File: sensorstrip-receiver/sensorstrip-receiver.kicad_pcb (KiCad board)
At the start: 2 copper layers, 40 x 12 mm, 8 parts, among them J1 Conn_01x02_MountingPin, J2 Conn_01x02_MountingPin

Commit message: fix humongous oversight
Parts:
- added ?: , , F.Cu at (133.2, 52.6)
- added ?: , , F.Cu at (105.0, 52.6)
- added ?: , , F.Cu at (106.9, 52.6)
- added ?: , , F.Cu at (135.0, 52.8)
- moved D1 12.0 mm to (114.0, 58.5)
- moved D3 12.0 mm to (126.0, 58.5)
- moved D2 0.50 mm to (120.0, 58.5)
- moved J2 0.10 mm to (106.0, 53.3)
- renumbered D3 to D1, D1 to D3
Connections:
- D1 pad 2: /LEDs -> /D1+
- D2 pad 1: GND -> /D1+
- D2 pad 2: /LEDs -> /D2+
- D3 pad 1: GND -> /D2+
- D3 pad 2: /LEDs -> /D3+
- R1 pad 1: /LEDs -> /D3+
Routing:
- net /LEDs: track 27.7 -> 0.00 mm
- net /D3+: track 0.00 -> 13.8 mm
- net GND: track 0.00 -> 6.47 mm, vias 4 -> 2
- net /D2+: track 0.00 -> 3.46 mm
- net /D1+: track 0.00 -> 3.46 mm
- net Power_postSwitch: track 9.28 -> 8.10 mm, vias 3 -> 1
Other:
- board size 40 x 12 mm -> 40 x 12.5 mm
- board text added: "+"
- board text added: "-"

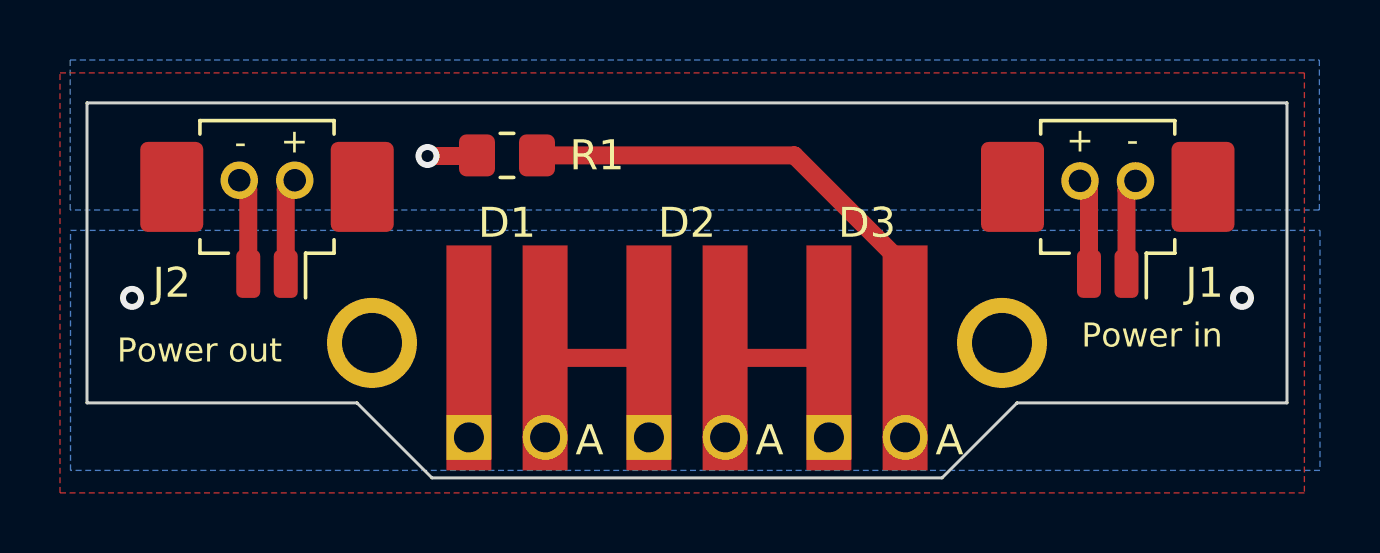
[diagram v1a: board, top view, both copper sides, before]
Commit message: Cleanup in preparation for push
Update project files to KiCad 7 format
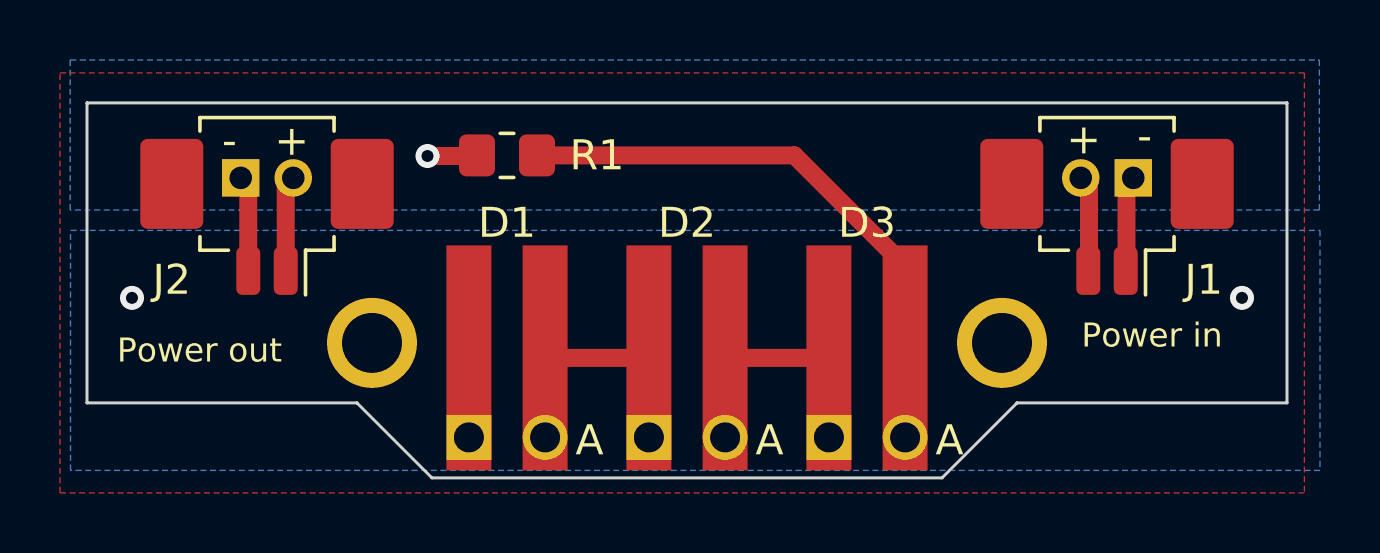
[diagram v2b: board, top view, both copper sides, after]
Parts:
- removed the ? at (133.2, 52.6)
- removed the ? at (105.0, 52.6)
- removed the ? at (106.9, 52.6)
- removed the ? at (130.0, 59.4)
- removed the ? at (135.0, 52.8)
- added ?: MountingHole-2mm-PTH, sensorstrip:MountingHole-2mm-PTH, F.Cu at (130.5, 58.0)
- added REF**: Power-P1.75mm, sensorstrip:Power-P1.75mm, F.Cu at (106.0, 52.5)
- added REF**: Power-P1.75mm, sensorstrip:Power-P1.75mm, F.Cu at (134.0, 52.5)
- ?: value (none) -> MountingHole-2mm-PTH; footprint (none) -> sensorstrip:MountingHole-2mm-PTH
- moved ? 4.25 mm to (109.5, 58.0)
- moved J1 0.10 mm to (134.0, 53.2)
- moved J2 0.10 mm to (106.0, 53.2)
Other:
- board text removed: "+"
- board text removed: "-"

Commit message: Add 4IR+2IR switchable power board
Minor cleanup
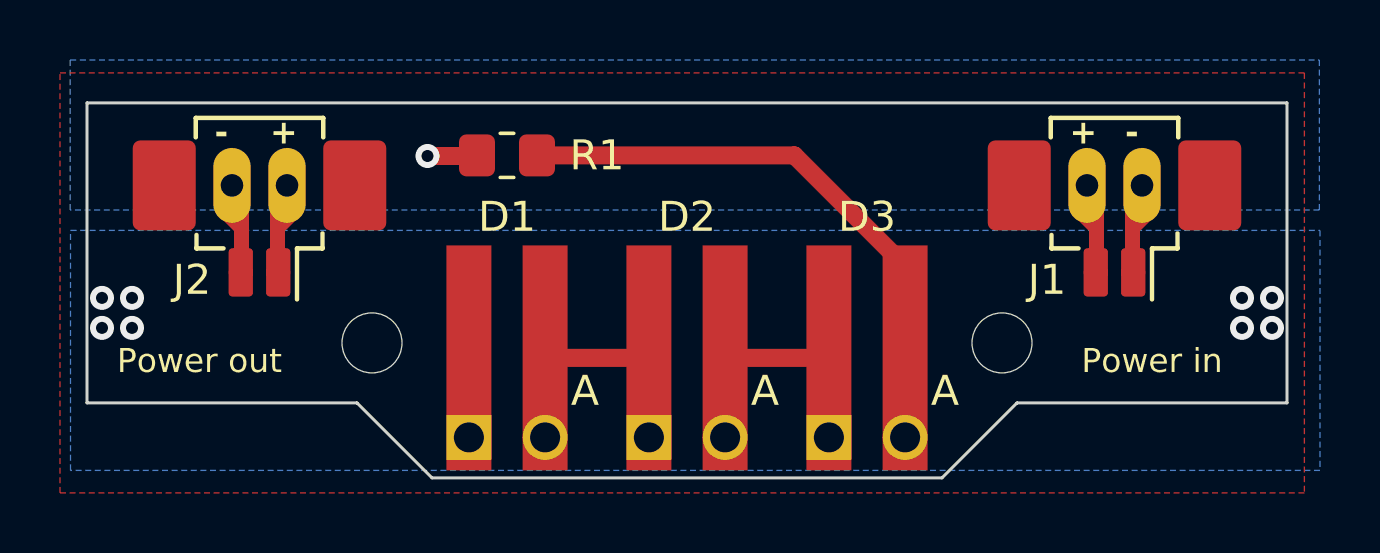
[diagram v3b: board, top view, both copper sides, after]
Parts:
- removed REF** (x2): Power-P1.75mm, sensorstrip:Power-P1.75mm
- ? (x2): value MountingHole-2mm-PTH -> MountingHole-2mm-NPTH; footprint sensorstrip:MountingHole-2mm-PTH -> sensorstrip:MountingHole-2mm-NPTH
- J1, J2: footprint Connector_Molex:Molex_PicoBlade_53261-0271_1x02-1MP_P1.25mm_Horizontal -> sensorstrip:Molex_Picoblade_53261-0271-Hybrid
- moved J1 2.46 mm to (134.2, 55.6), turned to 0 degrees
- moved J2 2.46 mm to (105.8, 55.6), turned to 0 degrees
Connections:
- ? pad : GND -> (no net) (x2)
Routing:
- net Power_postSwitch: track 8.10 -> 1.63 mm
- net GND: track 6.47 -> 0.00 mm, vias 2 -> 8
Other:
- board text added: "+"
- board text added: "-"
